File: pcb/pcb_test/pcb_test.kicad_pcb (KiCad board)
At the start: 2 copper layers, 98.5 x 66 mm, 57 parts, among them J1 Conn_02x04_Odd_Even, U1 MAX3221EIPWR, U2 LM324, U3 XIAO-ESP32-C3-DIP

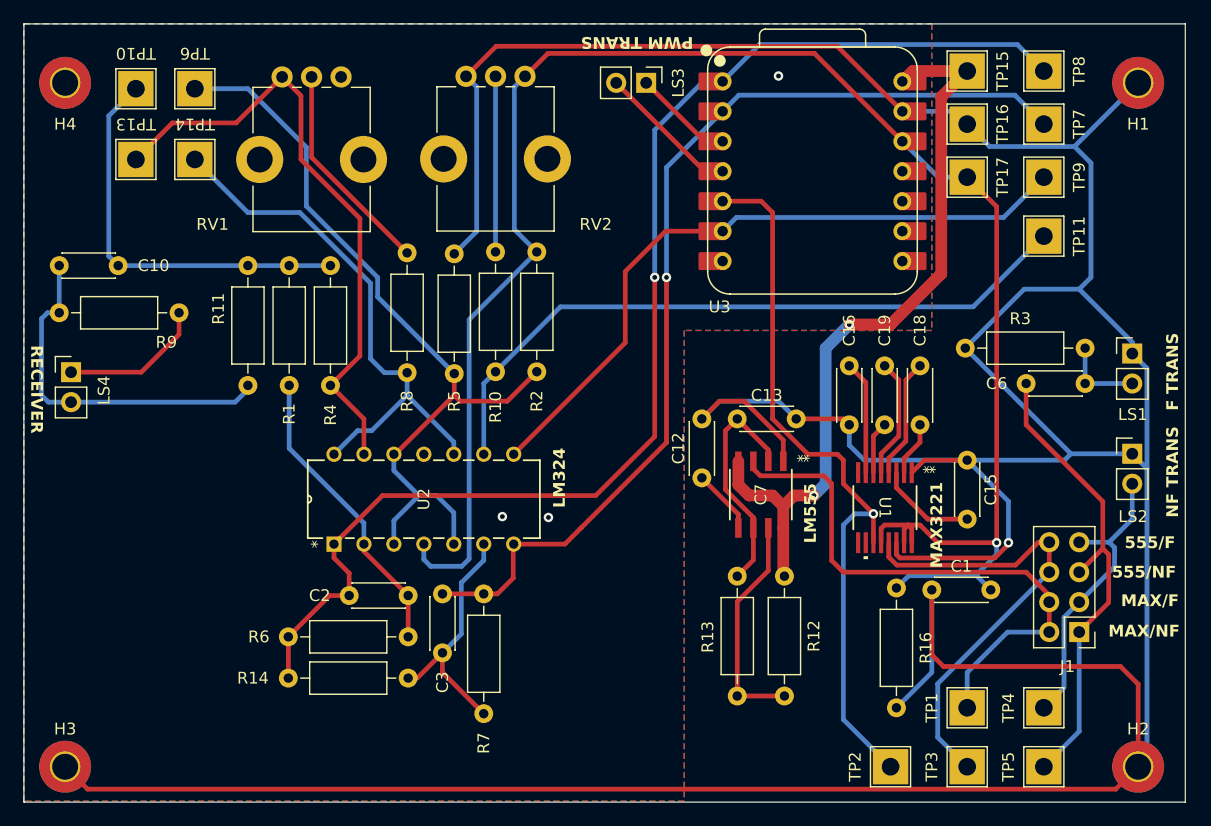
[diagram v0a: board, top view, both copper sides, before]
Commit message: fix: patch psb test issues and delete generated files
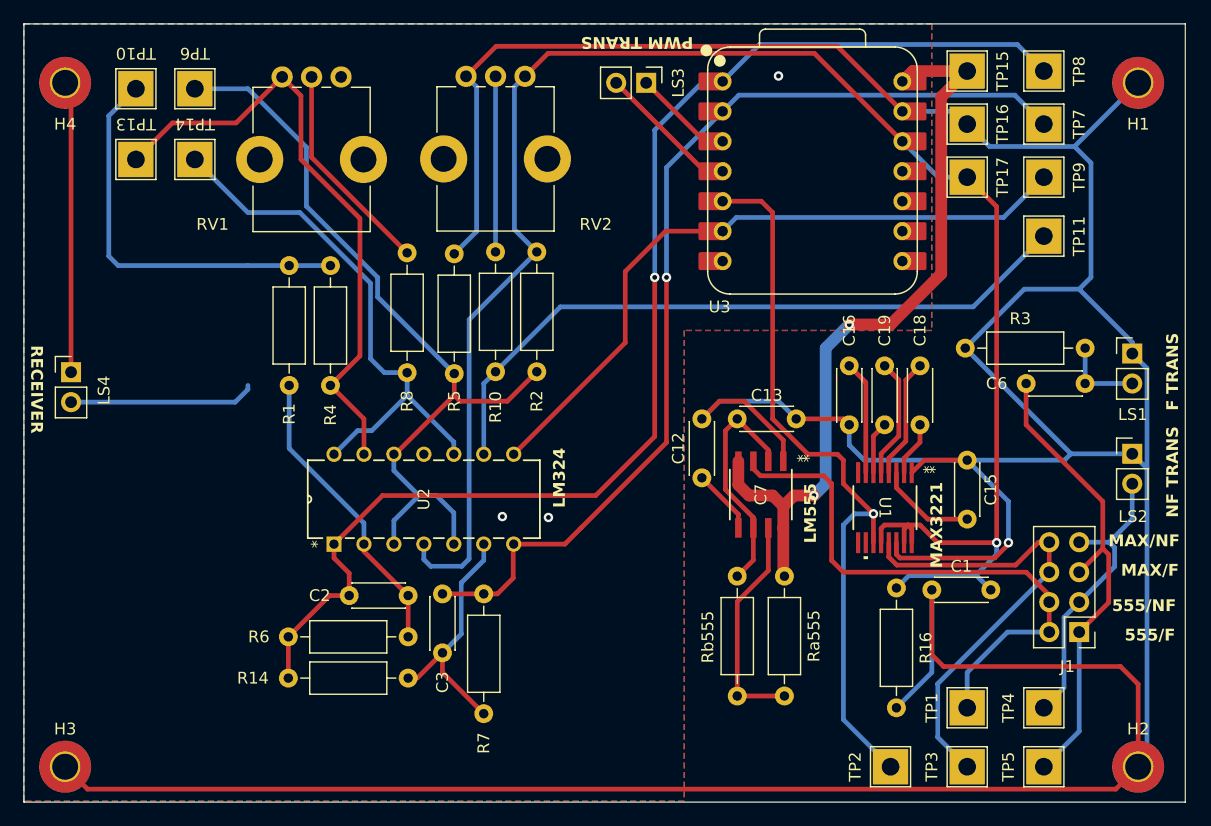
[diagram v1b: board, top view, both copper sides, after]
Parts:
- removed C10: 1nF, Capacitor_THT:C_Disc_D4.3mm_W1.9mm_P5.00mm
- removed R11: 0, Resistor_THT:R_Axial_DIN0207_L6.3mm_D2.5mm_P10.16mm_Horizontal
- removed R9: 4.7K, Resistor_THT:R_Axial_DIN0207_L6.3mm_D2.5mm_P10.16mm_Horizontal
- C1, C15, C16, C18, C19: value 0.1uF -> 100nF
- C6: value 1.7nF -> 1nF
- R1, R14, R4: value 220k -> 33k
- R10: value 220k -> 330k
- R16: value 100K -> 82k
- R2, R5: value 100k -> 330k
- R6, R7: value 220k -> 470k
- R8: value 220k -> 390k
- Rb555: renamed from R13; value 1.8M -> 1.2K
- renumbered R12 to Ra555
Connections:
- LS4 pad 1: Net-(LS4-Pad1) -> GND
- LS4 pad 2: Net-(C10-Pad1) -> trans_rcv
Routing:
- net Net-(C10-Pad1): track 30.7 -> 0.00 mm
- net GND: track 373.3 -> 398.0 mm
- net trans_rcv: track 34.3 -> 50.1 mm
- net Net-(LS4-Pad1): track 12.3 -> 0.00 mm

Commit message: fix: patch pcb design
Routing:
- net trans_rcv: track 50.1 -> 47.7 mm
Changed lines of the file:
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@@
 	)
 	(segment
-		(start 111.200001 54.379999)
-		(end 111.200001 66.280001)
+		(start 112 67.08)
+		(end 111.92 67.08)
 		(width 0.4)
 		(layer "B.Cu")
@@
 	)
 	(segment
-		(start 108 78.66)
-		(end 121.92 78.66)
+		(start 111 54.58)
+		(end 111 66.08)
+		(width 0.4)
+		(layer "B.Cu")
+		(net 14)
+	)
+	(segment
+		(start 111.92 67.08)
+		(end 111 68)
+		(width 0.4)
+		(layer "B.Cu")
+		(net 14)
+	)
+	(segment
+		(start 111 75.66)
+		(end 108 78.66)
 		(width 0.4)
 		(layer "B.Cu")
@@
 	)
 	(segment
-		(start 123 77.58)
-		(end 123 77.24)
-		(width 0.4)
-		(layer "B.Cu")
-		(net 14)
-	)
-	(segment
 		(start 112 67.08)
 		(end 123 67.08)
-		(width 0.4)
-		(layer "B.Cu")
-		(net 14)
-	)
-	(segment
-		(start 121.92 78.66)
-		(end 123 77.58)
 		(width 0.4)
 		(layer "B.Cu")
@@
 	)
 	(segment
-		(start 113.5 52.08)
-		(end 111.200001 54.379999)
+		(start 111 68)
+		(end 111 75.66)
 		(width 0.4)
 		(layer "B.Cu")
@@
 	)
 	(segment
-		(start 111.200001 66.280001)
+		(start 111 66.08)
 		(end 112 67.08)
 		(width 0.4)
 		(layer "B.Cu")
+		(net 14)
+	)
+	(segment
+		(start 113.5 52.08)
+		(end 111 54.58)
+		(width 0.4)
+		(layer "B.Cu")
